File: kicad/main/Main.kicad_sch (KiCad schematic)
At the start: 0 parts

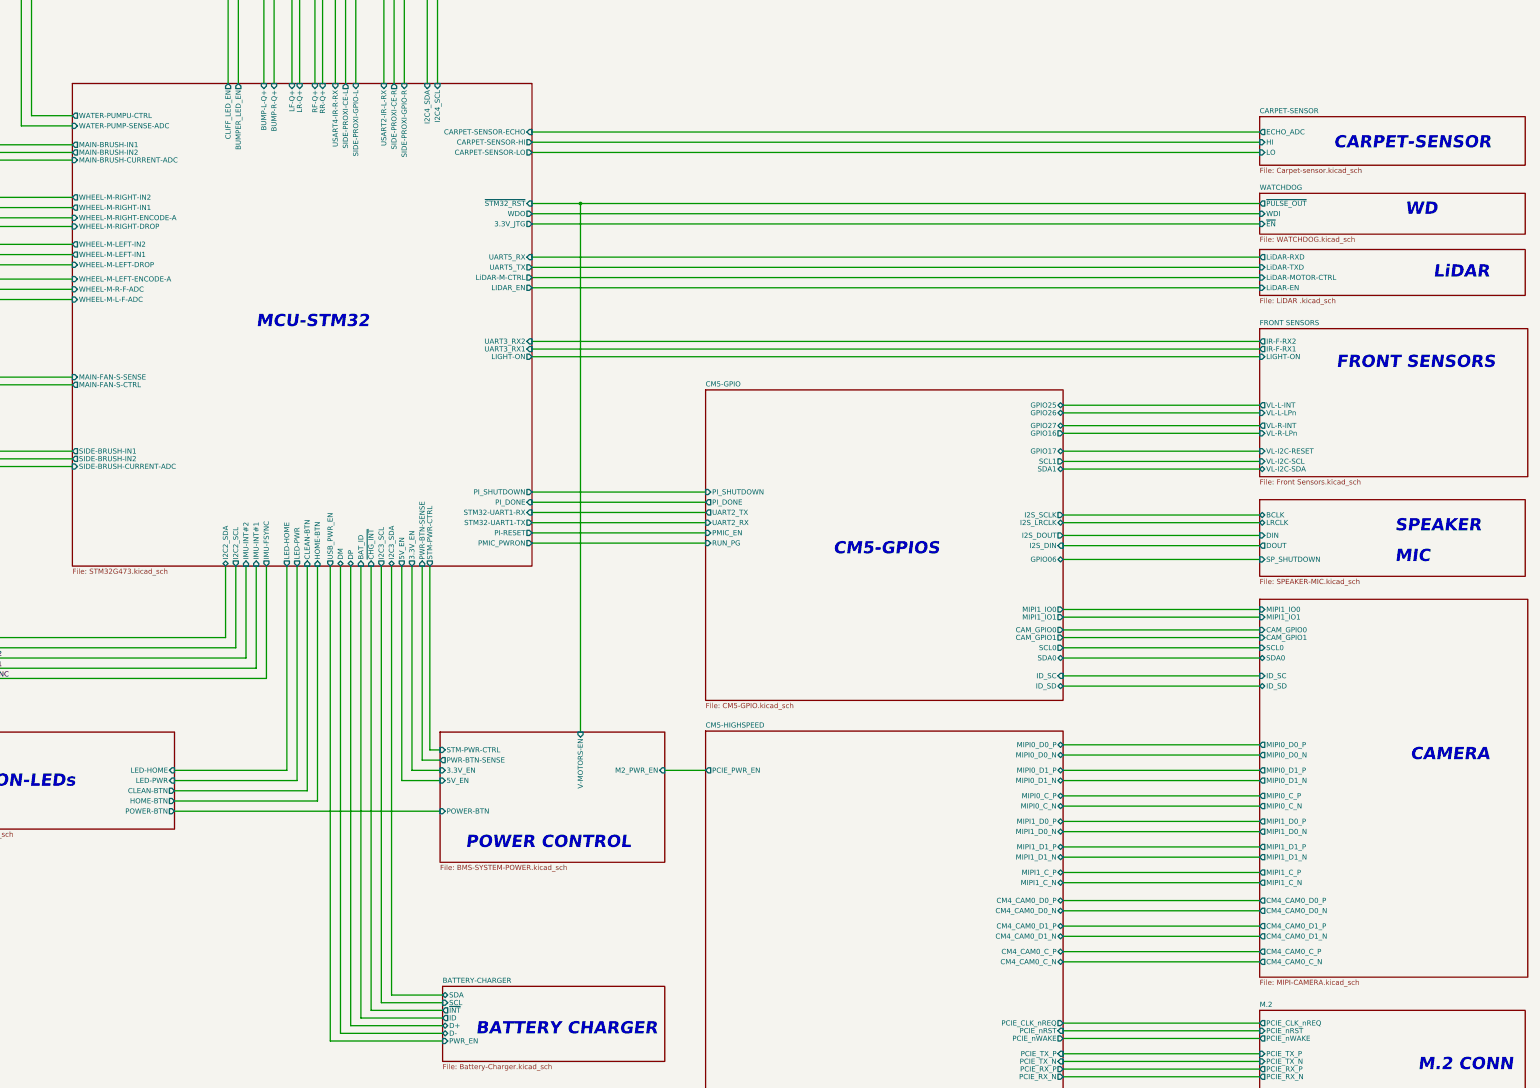
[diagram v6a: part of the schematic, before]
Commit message: Update Power Control sch, Charger sch, Speaker + Mic, JTAG and Watch Dog
**Power Control:** Replaced the BJT with a MOSFET. The MCU hang condition is not covered yet.
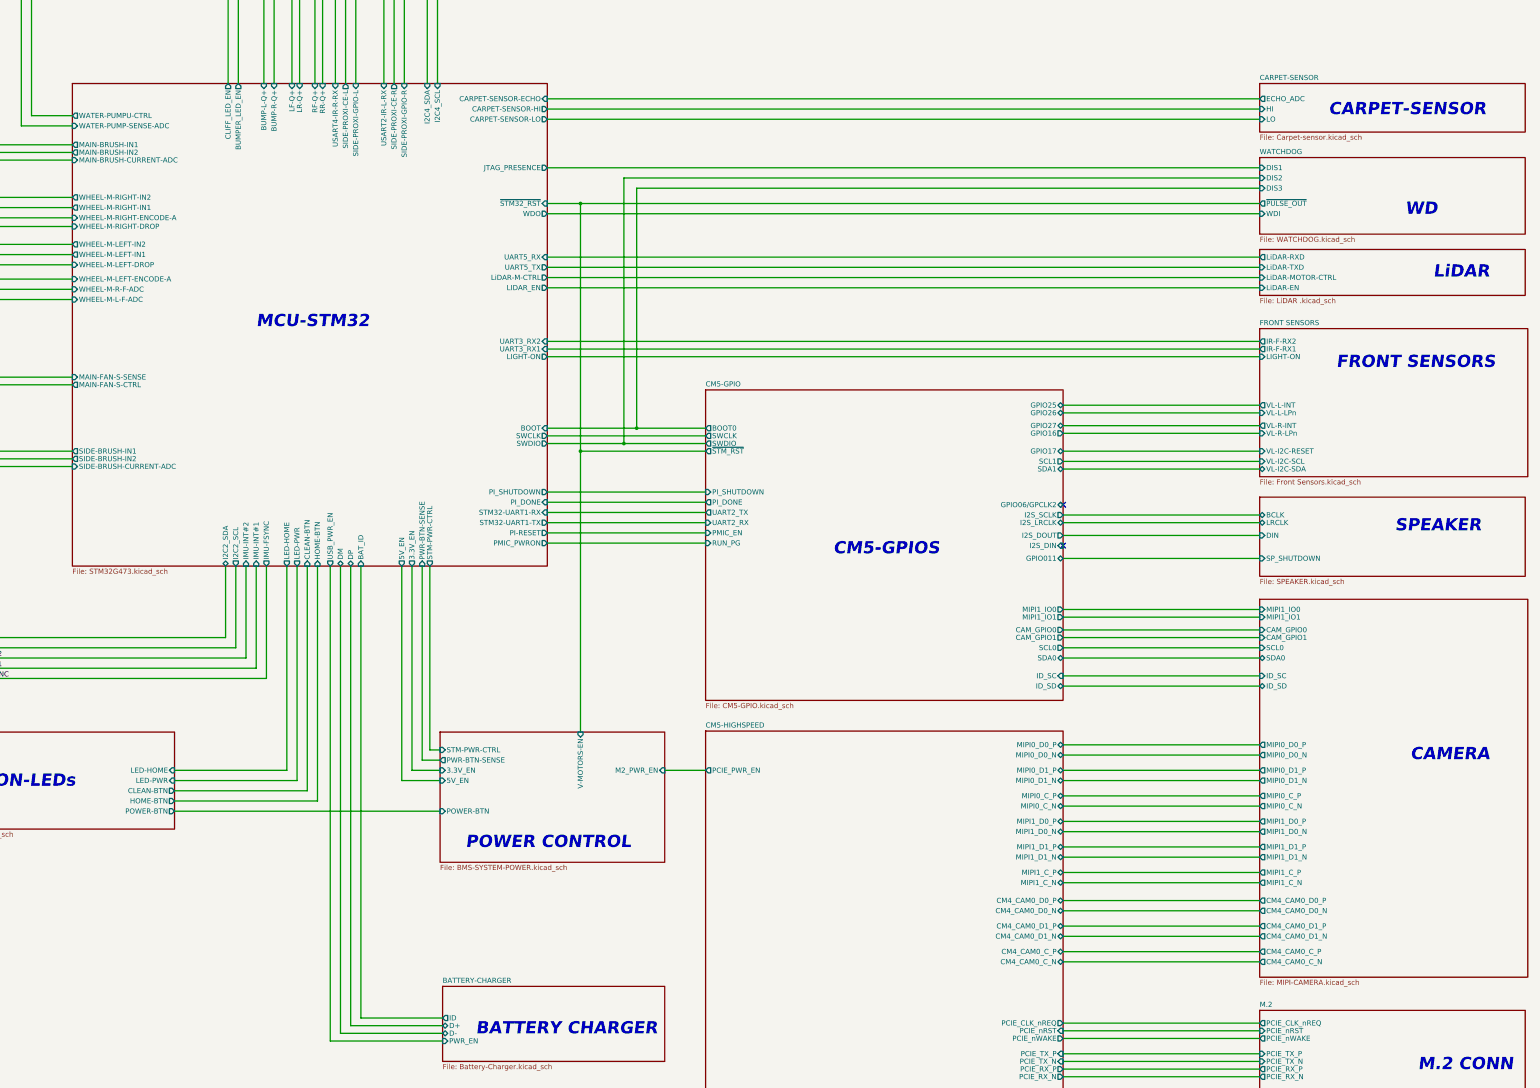
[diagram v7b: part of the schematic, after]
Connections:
- no-connect marks 0 -> 2
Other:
- sheet SPEAKER-MIC renamed SPEAKER
- sheet BATTERY-CHARGER ports: added none; removed SCL, SDA, ~{INT}
- sheet CM5-GPIO ports: added BOOT0, GPIO011, GPIO06/GPCLK2, SWCLK, SWDIO, ~{STM_RST}; removed GPIO06
- sheet MCU-STM32 ports: added BOOT, JTAG_PRESENCE, SWCLK, SWDIO; removed 3.3V_JTG, I2C3_SCL, I2C3_SDA, ~{CHG_INT}
- sheet SPEAKER: file SPEAKER-MIC.kicad_sch -> SPEAKER.kicad_sch
- sheet SPEAKER ports: added none; removed DOUT
- sheet WATCHDOG ports: added DIS1, DIS2, DIS3; removed ~{EN}
- note removed: "MIC"

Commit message: Cleaned up schematic filenames
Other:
- sheet CARPET-SENSOR ports: added none; removed HI
- sheet FRONT SENSORS: file Front Sensors.kicad_sch -> Front-Sensors.kicad_sch
- sheet LiDAR: file LiDAR .kicad_sch -> LiDAR.kicad_sch
- sheet MCU-STM32 ports: added ~{VM-VBAT-EN}; removed CARPET-SENSOR-HI
- sheet POWER: file BMS-SYSTEM-POWER.kicad_sch -> SYSTEM-POWER.kicad_sch
- sheet POWER ports: added ~{VM-VBAT-EN}; removed V-MOTORS-EN
- sheet WATER-PUMP: file WATER-PUMP .kicad_sch -> WATER-PUMP.kicad_sch
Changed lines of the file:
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@@
 	)
 	(junction
-		(at 274.955 205.74)
-		(diameter 0)
-		(color 0 0 0 0)
-	)
-	(junction
 		(at 285.75 203.835)
 		(diameter 0)
@@
 	(wire
 		(pts
-			(xy 266.7 120.65) (xy 443.865 120.65)
+			(xy 179.07 42.545) (xy 210.82 42.545)
 		)
 		(stroke
@@
 	(wire
 		(pts
-			(xy 179.07 42.545) (xy 210.82 42.545)
+			(xy 394.97 201.295) (xy 443.865 201.295)
 		)
 		(stroke
@@
 	(wire
 		(pts
-			(xy 394.97 201.295) (xy 443.865 201.295)
+			(xy 208.915 44.45) (xy 179.07 44.45)
 		)
 		(stroke
@@
 	(wire
 		(pts
-			(xy 208.915 44.45) (xy 179.07 44.45)
+			(xy 394.97 250.19) (xy 443.865 250.19)
 		)
 		(stroke
@@
 	(wire
 		(pts
-			(xy 394.97 250.19) (xy 443.865 250.19)
+			(xy 394.97 257.175) (xy 443.865 257.175)
 		)
 		(stroke
@@
 	(wire
 		(pts
-			(xy 394.97 257.175) (xy 443.865 257.175)
+			(xy 394.97 330.2) (xy 443.865 330.2)
 		)
 		(stroke
@@
 	(wire
 		(pts
-			(xy 394.97 330.2) (xy 443.865 330.2)
+			(xy 274.955 275.59) (xy 274.955 270.51)
 		)
 		(stroke
@@
 	(wire
 		(pts
-			(xy 274.955 205.74) (xy 274.955 275.59)
-		)
-		(stroke
-			(width 0)
-			(type default)
-		)
-	)
-	(wire
-		(pts
 			(xy 394.97 254.635) (xy 443.865 254.635)
 		)
@@
 	(wire
 		(pts
+			(xy 266.7 120.65) (xy 270.51 120.65)
+		)
+		(stroke
+			(width 0)
+			(type default)
+		)
+	)
+	(wire
+		(pts
 			(xy 179.07 64.135) (xy 187.325 64.135)
 		)
@@
 		)
 	)
+	(label "~{VM-VBAT-EN}"
+		(at 270.51 120.65 0)
+		(effects
+			(font
+				(size 1.27 1.27)
+			)
+			(justify left bottom)
+		)
+	)
+	(label "~{VM-VBAT-EN}"
+		(at 274.955 270.51 90)
+		(effects
+			(font
+				(size 1.27 1.27)
+			)
+			(justify left bottom)
+		)
+	)
 	(sheet
 		(at 306.07 275.336)
@@
 			)
 		)
-		(property "Sheetfile" "BMS-SYSTEM-POWER.kicad_sch"
+		(property "Sheetfile" "SYSTEM-POWER.kicad_sch"
 			(at 240.03 308.5596 0)
 			(show_name no)
@@
 			)
 		)
-		(pin "V-MOTORS-EN" input
+		(pin "~{VM-VBAT-EN}" input
 			(at 274.955 275.59 90)
 			(effects
@@
 			)
 		)
-		(pin "CARPET-SENSOR-HI" output
+		(pin "~{VM-VBAT-EN}" output
 			(at 266.7 120.65 0)
 			(effects
@@
 		)
 		(fill
-			(color 128 255 128 1)
+			(color 0 72 0 1)
 		)
 		(property "Sheetname" "LiDAR"
@@
 			)
 		)
-		(property "Sheetfile" "LiDAR .kicad_sch"
+		(property "Sheetfile" "LiDAR.kicad_sch"
 			(at 443.865 167.5896 0)
 			(show_name no)
@@
 		)
 		(fill
-			(color 128 255 128 1)
+			(color 0 72 0 1)
 		)
 		(property "Sheetname" "CARPET-SENSOR"
@@
 			)
 		)
-		(pin "HI" input
-			(at 443.865 120.65 180)
-			(effects
-				(font
-					(size 1.27 1.27)
-				)
-				(justify left)
-			)
-		)
 		(pin "LO" input
 			(at 443.865 123.19 180)
@@
 			)
 		)
-		(property "Sheetfile" "Front Sensors.kicad_sch"
+		(property "Sheetfile" "Front-Sensors.kicad_sch"
 			(at 443.865 212.6746 0)
 			(show_name no)
@@
 			)
 		)
-		(property "Sheetfile" "WATER-PUMP .kicad_sch"
+		(property "Sheetfile" "WATER-PUMP.kicad_sch"
 			(at 39.37 68.58 0)
 			(show_name no)
